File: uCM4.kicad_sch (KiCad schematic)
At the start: 39 parts, among them J1 Conn_01x03, J2 Ethernet, J3 Micro_SD_Card, J4 USB_B_Micro, SW1 SW_DIP_x01, SW2 SW_DIP_x01, U1 RT9742GGJ5, U2 74LVC1G07, U3 TPD4EUSB30

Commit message: Make preparations for required changes in 0.2.0
Following has been performed and could not be made separately:
- move LEDs to smaller space next to Ethernet
- move buttons to bigger space next to Ethernet
- two changes above makes together handy interface for whole board,
  where almost everything needed is on one side
- move all parts belonging to LEDs and buttons near their new locations
- change footprint of buffer chip to SOT-23-5, which is more likely to
  be used in this version
- reroute traces for all moved parts and do some small adjustments in
  other traces for easier routing (buttons not completed yet!)
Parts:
- U2: footprint Package_TO_SOT_SMD:SOT-353_SC-70-5_Handsoldering -> Package_TO_SOT_SMD:SOT-23-5_HandSoldering
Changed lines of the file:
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@@
       (effects (font (size 1.27 1.27)) (justify left))
     )
-    (property "Footprint" "Package_TO_SOT_SMD:SOT-353_SC-70-5_Handsoldering" (id 2) (at 148.59 182.88 0)
+    (property "Footprint" "Package_TO_SOT_SMD:SOT-23-5_HandSoldering" (id 2) (at 148.59 182.88 0)
       (effects (font (size 1.27 1.27)) hide)
     )
@@
     )
     (path "/25da1e56-3266-45da-a5a7-748f51f1532f"
-      (reference "U2") (unit 1) (value "74LVC1G07") (footprint "Package_TO_SOT_SMD:SOT-353_SC-70-5_Handsoldering")
+      (reference "U2") (unit 1) (value "74LVC1G07") (footprint "Package_TO_SOT_SMD:SOT-23-5_HandSoldering")
     )
     (path "/01206ff2-9474-4083-9f5e-454358df9096"

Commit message: Update footprint for buttons
Now should point to almost finished PTS840.
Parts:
- SW1, SW2: footprint Button_Switch_THT:SW_PUSH_6mm -> KiCAD_Randoms:PTS840_PM_SMTR_LFS
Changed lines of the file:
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@@
       (effects (font (size 1.27 1.27)) (justify right))
     )
-    (property "Footprint" "Button_Switch_THT:SW_PUSH_6mm" (id 2) (at 16.51 160.02 0)
+    (property "Footprint" "KiCAD_Randoms:PTS840_PM_SMTR_LFS" (id 2) (at 16.51 160.02 0)
       (effects (font (size 1.27 1.27)) hide)
     )
@@
     (property "Reference" "SW2" (id 0) (at 125.73 171.8268 0))
     (property "Value" "SW_DIP_x01" (id 1) (at 125.73 174.1255 0))
-    (property "Footprint" "Button_Switch_THT:SW_PUSH_6mm" (id 2) (at 125.73 177.8 0)
+    (property "Footprint" "KiCAD_Randoms:PTS840_PM_SMTR_LFS" (id 2) (at 125.73 177.8 0)
       (effects (font (size 1.27 1.27)) hide)
     )
@@
     )
     (path "/53e986ab-59c5-4be6-a04f-f5936095ef65"
-      (reference "SW1") (unit 1) (value "SW_DIP_x01") (footprint "Button_Switch_THT:SW_PUSH_6mm")
+      (reference "SW1") (unit 1) (value "SW_DIP_x01") (footprint "KiCAD_Randoms:PTS840_PM_SMTR_LFS")
     )
     (path "/311375dd-fa64-4cb4-aaf9-68277d25563b"
-      (reference "SW2") (unit 1) (value "SW_DIP_x01") (footprint "Button_Switch_THT:SW_PUSH_6mm")
+      (reference "SW2") (unit 1) (value "SW_DIP_x01") (footprint "KiCAD_Randoms:PTS840_PM_SMTR_LFS")
     )
     (path "/c771086f-6945-446c-a2ff-681ac70e1440"

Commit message: Power buttons - issue #7
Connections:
- net ACT_LED: now reaches Module1.21 (PI_nLED_Activity), R15.1
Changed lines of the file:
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@@
   (junction (at 167.005 43.18) (diameter 1.016) (color 0 0 0 0))
   (junction (at 167.64 53.34) (diameter 1.016) (color 0 0 0 0))
+  (junction (at 170.18 30.48) (diameter 1.016) (color 0 0 0 0))
   (junction (at 171.45 71.755) (diameter 1.016) (color 0 0 0 0))
   (junction (at 186.69 52.07) (diameter 1.016) (color 0 0 0 0))
@@
     (stroke (width 0) (type solid) (color 0 0 0 0))
   )
-  (wire (pts (xy 124.46 30.48) (xy 171.45 30.48))
+  (wire (pts (xy 124.46 30.48) (xy 170.18 30.48))
     (stroke (width 0) (type solid) (color 0 0 0 0))
   )
@@
   )
   (wire (pts (xy 167.64 186.69) (xy 167.64 194.31))
+    (stroke (width 0) (type solid) (color 0 0 0 0))
+  )
+  (wire (pts (xy 170.18 25.4) (xy 170.18 30.48))
+    (stroke (width 0) (type solid) (color 0 0 0 0))
+  )
+  (wire (pts (xy 170.18 30.48) (xy 171.45 30.48))
     (stroke (width 0) (type solid) (color 0 0 0 0))
   )
@@
     (effects (font (size 1.27 1.27)) (justify left bottom))
   )
+  (label "ACT_LED" (at 170.18 25.4 0)
+    (effects (font (size 1.27 1.27)) (justify left bottom))
+  )

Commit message: Add LCSC# to symbols
Still connectors are missing them, but allows generating BOM as good as
present in repo - manual one.
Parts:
- C1: LCSC# (none) -> C19702
- C2: LCSC# (none) -> C14663
- D1: LCSC# (none) -> C2286
- D2: LCSC# (none) -> C72043
- R1: LCSC# (none) -> C22962
- R10, R11, R6, R7, R8, R9: LCSC# (none) -> C17168
- R12, R14: LCSC# (none) -> C23179
- R13, R15: LCSC# (none) -> C21190
- R3, R4: LCSC# (none) -> C21189
- R5: LCSC# (none) -> C22790
- U1: LCSC# (none) -> C2693603
- U2: LCSC# (none) -> C67531
- U3: LCSC# (none) -> C558427
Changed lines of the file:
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@@
+      (effects (font (size 1.27 1.27)) hide)
+    )
+    (property "LCSC#" "C22962" (id 4) (at 16.51 173.99 0)
       (effects (font (size 1.27 1.27)) hide)
     )
@@
       (effects (font (size 1.27 1.27)) hide)
     )
+    (property "LCSC#" "C21189" (id 4) (at 27.94 62.23 0)
+      (effects (font (size 1.27 1.27)) hide)
+    )
     (pin "1")
     (pin "2")
@@
       (effects (font (size 1.27 1.27)) hide)
     )
+    (property "LCSC#" "C21189" (id 4) (at 27.94 120.65 0)
+      (effects (font (size 1.27 1.27)) hide)
+    )
     (pin "1")
     (pin "2")
@@
     )
     (property "Datasheet" "~" (id 3) (at 118.11 142.24 0)
+      (effects (font (size 1.27 1.27)) hide)
+    )
+    (property "LCSC#" "C22790" (id 4) (at 118.11 142.24 0)
       (effects (font (size 1.27 1.27)) hide)
     )
@@
       (effects (font (size 1.27 1.27)) hide)
     )
+    (property "LCSC#" "C17168" (id 4) (at 132.08 111.76 0)
+      (effects (font (size 1.27 1.27)) hide)
+    )
     (pin "1")
     (pin "2")
@@
       (effects (font (size 1.27 1.27)) hide)
     )
+    (property "LCSC#" "C17168" (id 4) (at 132.08 114.3 0)
+      (effects (font (size 1.27 1.27)) hide)
+    )
     (pin "1")
     (pin "2")
@@
       (effects (font (size 1.27 1.27)) hide)
     )
+    (property "LCSC#" "C17168" (id 4) (at 132.08 116.84 0)
+      (effects (font (size 1.27 1.27)) hide)
+    )
     (pin "1")
     (pin "2")
@@
       (effects (font (size 1.27 1.27)) hide)
     )
+    (property "LCSC#" "C17168" (id 4) (at 132.08 121.92 0)
+      (effects (font (size 1.27 1.27)) hide)
+    )
     (pin "1")
     (pin "2")
@@
       (effects (font (size 1.27 1.27)) hide)
     )
+    (property "LCSC#" "C17168" (id 4) (at 132.08 127 0)
+      (effects (font (size 1.27 1.27)) hide)
+    )
     (pin "1")
     (pin "2")
@@
       (effects (font (size 1.27 1.27)) hide)
     )
+    (property "LCSC#" "C17168" (id 4) (at 132.08 129.54 0)
+      (effects (font (size 1.27 1.27)) hide)
+    )
     (pin "1")
     (pin "2")
@@
       (effects (font (size 1.27 1.27)) hide)
     )
+    (property "LCSC#" "C23179" (id 4) (at 142.24 81.915 0)
+      (effects (font (size 1.27 1.27)) hide)
+    )
     (pin "1")
     (pin "2")
@@
       (effects (font (size 1.27 1.27)) hide)
     )
+    (property "LCSC#" "C23179" (id 4) (at 149.86 81.915 0)
+      (effects (font (size 1.27 1.27)) hide)
+    )
     (pin "1")
     (pin "2")
@@
       (effects (font (size 1.27 1.27)) hide)
     )
+    (property "LCSC#" "C21190" (id 4) (at 152.4 194.31 0)
+      (effects (font (size 1.27 1.27)) hide)
+    )
     (pin "1")
     (pin "2")
@@
     )
     (property "Datasheet" "~" (id 3) (at 175.26 30.48 0)
+      (effects (font (size 1.27 1.27)) hide)
+    )
+    (property "LCSC#" "C21190" (id 4) (at 175.26 30.48 0)
       (effects (font (size 1.27 1.27)) hide)
     )
@@
       (effects (font (size 1.27 1.27)) hide)
     )
+    (property "LCSC#" "C2286" (id 4) (at 163.83 194.31 0)
+      (effects (font (size 1.27 1.27)) hide)
+    )
     (pin "1")
     (pin "2")
@@
       (effects (font (size 1.27 1.27)) hide)
     )
+    (property "LCSC#" "C72043" (id 4) (at 186.69 30.48 0)
+      (effects (font (size 1.27 1.27)) hide)
+    )
     (pin "1")
     (pin "2")
@@
       (effects (font (size 1.27 1.27)) hide)
     )
+    (property "LCSC#" "C19702" (id 4) (at 109.22 144.78 0)
+      (effects (font (size 1.27 1.27)) hide)
+    )
     (pin "1")
     (pin "2")
@@
     )
     (property "Datasheet" "~" (id 3) (at 171.45 83.185 0)
+      (effects (font (size 1.27 1.27)) hide)
+    )
+    (property "LCSC#" "C14663" (id 4) (at 171.45 83.185 0)
       (effects (font (size 1.27 1.27)) hide)
     )
@@
       (effects (font (size 1.27 1.27)) hide)
     )
+    (property "LCSC#" "C67531" (id 4) (at 148.59 182.88 0)
+      (effects (font (size 1.27 1.27)) hide)
+    )
     (pin "2")
     (pin "3")
@@
     )
     (property "Part Description" "	Power Switch/Driver 1:1 N-Channel 1A TSOT-23-5" (id 9) (at 133.35 137.16 0)
+      (effects (font (size 1.27 1.27)) hide)
+    )
+    (property "LCSC#" "C2693603" (id 10) (at 133.35 137.16 0)
       (effects (font (size 1.27 1.27)) hide)
     )
@@
       (effects (font (size 1.27 1.27)) hide)
     )
+    (property "LCSC#" "C558427" (id 4) (at 267.97 68.58 0)
+      (effects (font (size 1.27 1.27)) hide)
+    )

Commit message: Fill LCSC part numbers for connectors
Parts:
- J1: LCSC# (none) -> C49257
- J2: LCSC# (none) -> C363232
- J3: LCSC# (none) -> C113206
- J4: LCSC# (none) -> C2682232
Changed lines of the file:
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@@
+      (effects (font (size 1.27 1.27)) hide)
+    )
+    (property "LCSC#" "C49257" (id 4) (at 123.19 97.79 0)
       (effects (font (size 1.27 1.27)) hide)
     )
@@
       (effects (font (size 1.27 1.27)) hide)
     )
+    (property "LCSC#" "C2682232" (id 4) (at 265.43 41.91 0)
+      (effects (font (size 1.27 1.27)) hide)
+    )
     (pin "1")
     (pin "2")
@@
       (effects (font (size 1.27 1.27)) hide)
     )
+    (property "LCSC#" "C363232" (id 4) (at 129.54 35.56 0)
+      (effects (font (size 1.27 1.27)) hide)
+    )
     (pin "L1")
     (pin "L2")
@@
       (effects (font (size 1.27 1.27)) hide)
     )
+    (property "LCSC#" "C113206" (id 4) (at 160.02 121.92 0)
+      (effects (font (size 1.27 1.27)) hide)
+    )

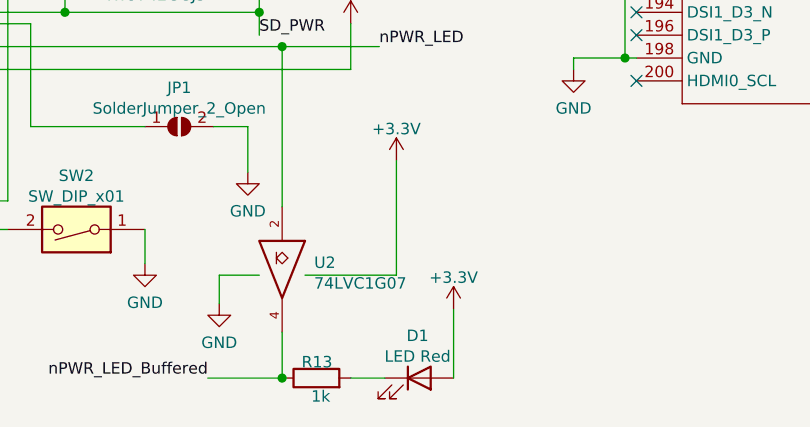
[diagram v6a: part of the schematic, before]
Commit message: Update part names and add LCSC#
For 74LVC1G07 buffer and power+reset buttons.
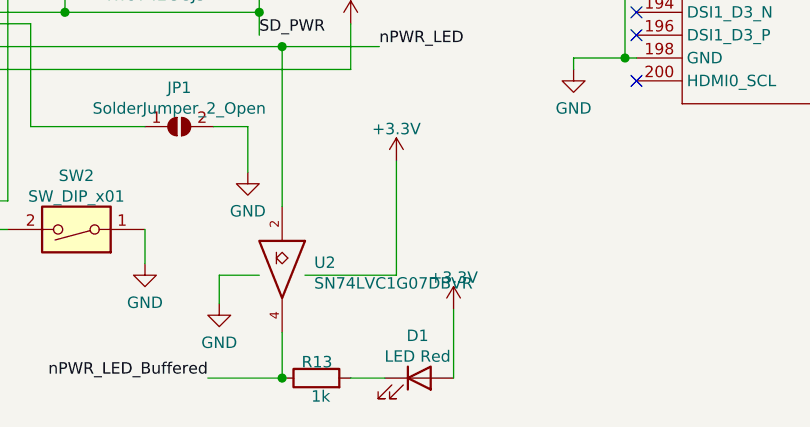
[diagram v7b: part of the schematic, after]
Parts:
- SW1, SW2: LCSC# (none) -> C221911
- U2: value 74LVC1G07 -> SN74LVC1G07DBVR; LCSC# C67531 -> C7829
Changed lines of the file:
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@@
+      (effects (font (size 1.27 1.27)) hide)
+    )
+    (property "LCSC#" "C221911" (id 4) (at 16.51 160.02 90)
       (effects (font (size 1.27 1.27)) hide)
     )
@@
       (effects (font (size 1.27 1.27)) hide)
     )
+    (property "LCSC#" "C221911" (id 4) (at 125.73 177.8 0)
+      (effects (font (size 1.27 1.27)) hide)
+    )
     (pin "1")
     (pin "2")
@@
       (effects (font (size 1.27 1.27)) (justify left))
     )
-    (property "Value" "74LVC1G07" (id 1) (at 152.1461 183.7828 90)
+    (property "Value" "SN74LVC1G07DBVR" (id 1) (at 152.1461 183.7828 90)
       (effects (font (size 1.27 1.27)) (justify left))
     )
@@
       (effects (font (size 1.27 1.27)) hide)
     )
-    (property "LCSC#" "C67531" (id 4) (at 148.59 182.88 0)
+    (property "LCSC#" "C7829" (id 4) (at 148.59 182.88 0)
       (effects (font (size 1.27 1.27)) hide)
     )
@@
     )
     (path "/25da1e56-3266-45da-a5a7-748f51f1532f"
-      (reference "U2") (unit 1) (value "74LVC1G07") (footprint "Package_TO_SOT_SMD:SOT-23-5_HandSoldering")
+      (reference "U2") (unit 1) (value "SN74LVC1G07DBVR") (footprint "Package_TO_SOT_SMD:SOT-23-5_HandSoldering")
     )
     (path "/01206ff2-9474-4083-9f5e-454358df9096"

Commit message: Commit missed jumper on schematics
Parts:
- JP1: footprint Special:Jumper -> Jumper:SolderJumper-2_P1.3mm_Open_RoundedPad1.0x1.5mm
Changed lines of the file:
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@@
     (property "Reference" "JP1" (id 0) (at 137.16 162.0478 0))
     (property "Value" "SolderJumper_2_Open" (id 1) (at 137.16 164.3465 0))
-    (property "Footprint" "Special:Jumper" (id 2) (at 137.16 166.37 0)
+    (property "Footprint" "Jumper:SolderJumper-2_P1.3mm_Open_RoundedPad1.0x1.5mm" (id 2) (at 137.16 166.37 0)
       (effects (font (size 1.27 1.27)) hide)
     )
@@
     )
     (path "/debd560e-0565-4cbf-9569-5f25352bd66e"
-      (reference "JP1") (unit 1) (value "SolderJumper_2_Open") (footprint "Special:Jumper")
+      (reference "JP1") (unit 1) (value "SolderJumper_2_Open") (footprint "Jumper:SolderJumper-2_P1.3mm_Open_RoundedPad1.0x1.5mm")
     )
     (path "/6e99bc10-5f29-45d8-a271-3de00e4eb307"
